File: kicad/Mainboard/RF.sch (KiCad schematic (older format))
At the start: 96 parts, among them J8 Antenna, Q3 BGA6589, T1 AFT05MS004NT1, U5 ADF7021, U6 HMC546MS8GETR, U7 LM2904A, X1 12.288MHz

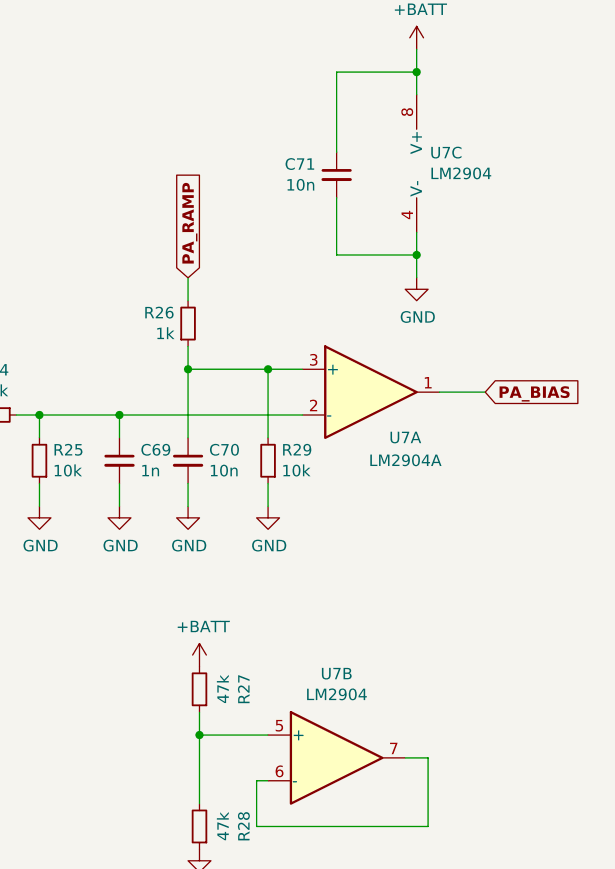
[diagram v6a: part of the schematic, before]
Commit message: Add files via upload
fixed U7 name (LM2904A)
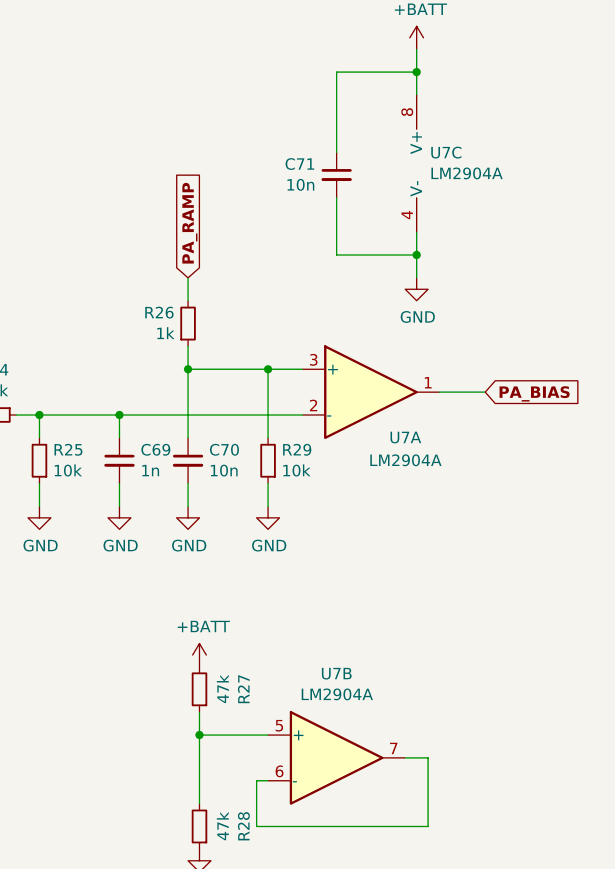
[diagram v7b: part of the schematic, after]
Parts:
- U7: value LM2904 -> LM2904A
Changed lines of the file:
@@
 P 14350 3300
 F 0 "U7" H 14308 3346 50  0000 L CNN
-F 1 "LM2904" H 14308 3255 50  0000 L CNN
+F 1 "LM2904A" H 14308 3255 50  0000 L CNN
 F 2 "Package_SO:SO-8_3.9x4.9mm_P1.27mm" H 14350 3300 50  0001 C CNN
 F 3 "http://www.ti.com/lit/ds/symlink/lm358.pdf" H 14350 3300 50  0001 C CNN
@@
 P 13900 5900
 F 0 "U7" H 13900 6267 50  0000 C CNN
-F 1 "LM2904" H 13900 6176 50  0000 C CNN
+F 1 "LM2904A" H 13900 6176 50  0000 C CNN
 F 2 "Package_SO:SO-8_3.9x4.9mm_P1.27mm" H 13900 5900 50  0001 C CNN
 F 3 "http://www.ti.com/lit/ds/symlink/lm358.pdf" H 13900 5900 50  0001 C CNN

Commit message: - Added footprint library - TR-9 - Imported a few footprints - Designed a MicroSD card slot footprint - Assignment footprints to corresponding elements on schematic
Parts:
- Q3: footprint (none) -> TR-9:BGA6589
- T1: footprint (none) -> TR-9:AFT05MS004NT1
- X1: footprint (none) -> TR-9:ECS-TXO-3225
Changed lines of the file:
@@
 EESchema Schematic File Version 4
-LIBS:Mainboard-cache
 EELAYER 30 0
 EELAYER END
@@
 F 0 "T1" H 6394 2953 59  0000 L CNN
 F 1 "AFT05MS004NT1" H 5950 2100 59  0000 L CNN
-F 2 "" H 6250 2900 50  0001 C CNN
+F 2 "TR-9:AFT05MS004NT1" H 6250 2900 50  0001 C CNN
 F 3 "" H 6250 2900 50  0001 C CNN
 	1    6250 2900
@@
 F 0 "X1" H 6950 7000 50  0000 R CNN
 F 1 "12.288MHz" H 6950 6900 50  0000 R CNN
-F 2 "" H 7100 6900 50  0001 C CNN
+F 2 "TR-9:ECS-TXO-3225" H 7100 6900 50  0001 C CNN
 F 3 "" H 6900 7350 50  0001 C CNN
 	1    7100 7250
@@
 F 0 "Q3" H 3850 3481 79  0000 C CNN
 F 1 "BGA6589" H 3850 3346 79  0000 C CNN
-F 2 "" H 3850 4350 79  0001 C CNN
+F 2 "TR-9:BGA6589" H 3850 4350 79  0001 C CNN
 F 3 "" H 3850 4350 79  0001 C CNN
 	1    3850 3000
